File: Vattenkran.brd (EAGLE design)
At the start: 65 x 80 mm, 13 parts, among them Q2 32KHz

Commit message: Replaced crystal
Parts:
- removed Q2: 32KHz, adafruit:TC38H
- added U$2: 32Khz, Semiconductors:SM3
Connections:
- net N$4: now also U$2.P$1; no longer Q2.2
- net N$5: now also U$2.P$2; no longer Q2.1
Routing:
- net N$4: track 6.17 -> 5.39 mm
- net N$5: track 6.08 -> 5.39 mm
- net SUPERCAP: track 5.10 -> 4.45 mm
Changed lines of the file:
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@@
 <element name="C3" library="resistor" library_urn="urn:adsk.eagle:library:348" package="C0805" package3d_urn="urn:adsk.eagle:package:26137/1" value="100nF" x="16.5" y="57.5" rot="MR90"/>
 <element name="LED2" library="led" library_urn="urn:adsk.eagle:library:259" package="LED3MM" package3d_urn="urn:adsk.eagle:package:15797/1" value="GREEN" x="15.63" y="16.18" rot="R90"/>
-<element name="Q2" library="adafruit" package="TC38H" value="32KHz" x="39.23" y="72.42" rot="R180">
-<attribute name="MF" value="" x="39.23" y="72.42" size="1.778" layer="27" rot="R180" display="off"/>
-<attribute name="MPN" value="" x="39.23" y="72.42" size="1.778" layer="27" rot="R180" display="off"/>
-<attribute name="OC_FARNELL" value="unknown" x="39.23" y="72.42" size="1.778" layer="27" rot="R180" display="off"/>
-<attribute name="OC_NEWARK" value="unknown" x="39.23" y="72.42" size="1.778" layer="27" rot="R180" display="off"/>
-</element>
 <element name="R2" library="resistor" library_urn="urn:adsk.eagle:library:348" package="R0805" package3d_urn="urn:adsk.eagle:package:26059/1" value="3K3" x="15.63" y="22.2" rot="MR90"/>
 <element name="SUPERCAP" library="rcl" library_urn="urn:adsk.eagle:library:334" package="ETR2" package3d_urn="urn:adsk.eagle:package:23315/1" value="1F" x="31.8" y="64.02" rot="R180">
@@
 <attribute name="TP_SIGNAL_NAME" value="" x="0" y="60" size="1.778" layer="28" rot="MR0" display="off"/>
 </element>
+<element name="U$2" library="Semiconductors" package="SM3" value="32Khz" x="39.5" y="72" rot="MR270"/>
 </elements>
 <signals>
@@
 <contactref element="U$1" pad="8"/>
 <contactref element="SUPERCAP" pad="+"/>
-<wire x1="37.595" y1="61.14" x2="36.36" y2="61.14" width="0.6096" layer="16"/>
-<wire x1="36.36" y1="61.14" x2="35.34" y2="63.66" width="0.6096" layer="16"/>
-<wire x1="35.34" y1="63.66" x2="34.7" y2="63.66" width="0.6096" layer="16"/>
-<wire x1="34.7" y1="63.66" x2="34.34" y2="64.02" width="0.6096" layer="16"/>
+<wire x1="34.34" y1="64.02" x2="37.22" y2="61.14" width="0.4064" layer="16"/>
+<wire x1="37.22" y1="61.14" x2="37.595" y2="61.14" width="0.4064" layer="16"/>
 </signal>
 <signal name="BT_STATE">
@@
 </signal>
 <signal name="N$4">
-<contactref element="Q2" pad="2"/>
 <contactref element="U$1" pad="2"/>
-<wire x1="38.865" y1="66.86" x2="38.865" y2="71.635" width="0.4064" layer="16"/>
-<wire x1="37.96" y1="72.54" x2="37.96" y2="72.42" width="0.4064" layer="16"/>
-<wire x1="38.865" y1="71.635" x2="37.96" y2="72.54" width="0.4064" layer="16"/>
+<contactref element="U$2" pad="P$1"/>
+<wire x1="38.865" y1="66.86" x2="38.865" y2="69.635" width="0.4064" layer="16"/>
+<wire x1="38.25" y1="70.25" x2="38.25" y2="72" width="0.4064" layer="16"/>
+<wire x1="38.865" y1="69.635" x2="38.25" y2="70.25" width="0.4064" layer="16"/>
 </signal>
 <signal name="N$5">
 <contactref element="U$1" pad="3"/>
-<contactref element="Q2" pad="1"/>
-<wire x1="40.135" y1="66.86" x2="40.135" y2="72.555" width="0.4064" layer="16"/>
-<wire x1="40.135" y1="72.555" x2="40.5" y2="72.42" width="0.4064" layer="16"/>
+<contactref element="U$2" pad="P$2"/>
+<wire x1="40.135" y1="66.86" x2="40.135" y2="69.635" width="0.4064" layer="16"/>
+<wire x1="40.75" y1="70.25" x2="40.75" y2="72" width="0.4064" layer="16"/>
+<wire x1="40.135" y1="69.635" x2="40.75" y2="70.25" width="0.4064" layer="16"/>
 </signal>
 <signal name="VALVE_ENABLE">

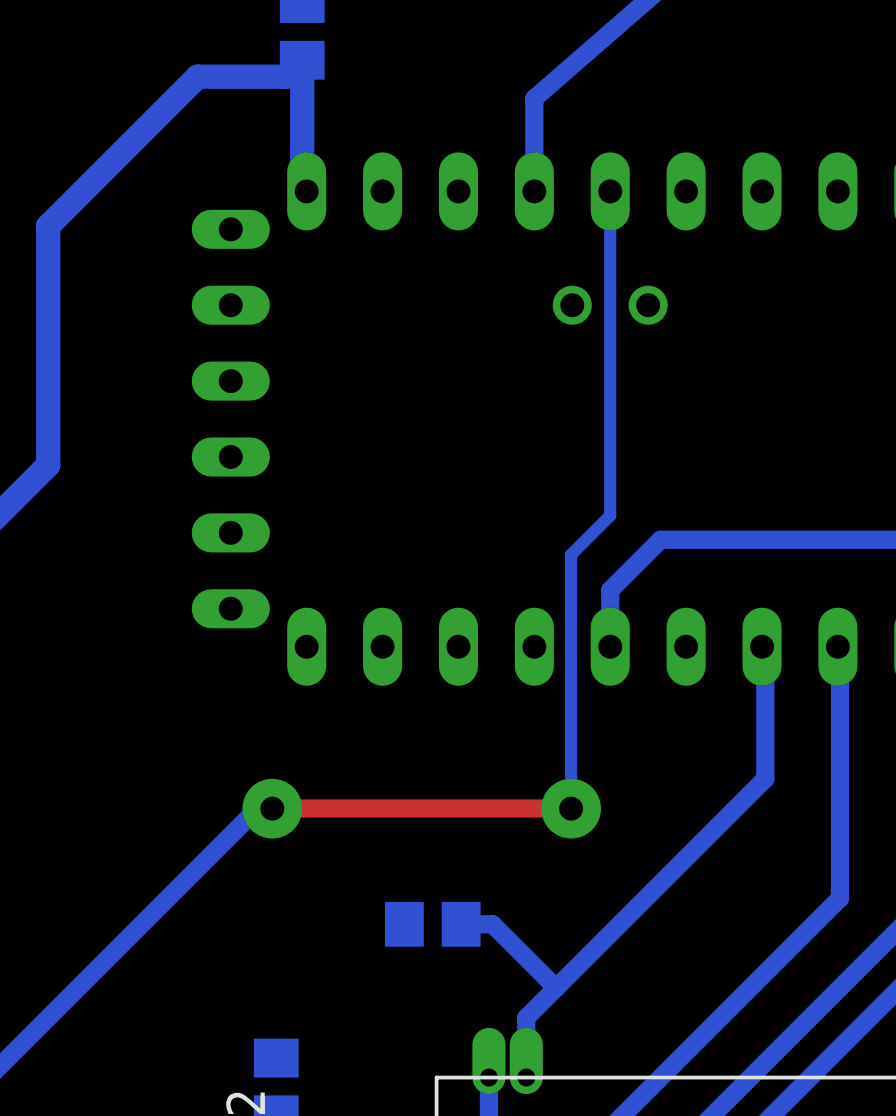
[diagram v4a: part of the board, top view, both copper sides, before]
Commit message: Fixed thermals size
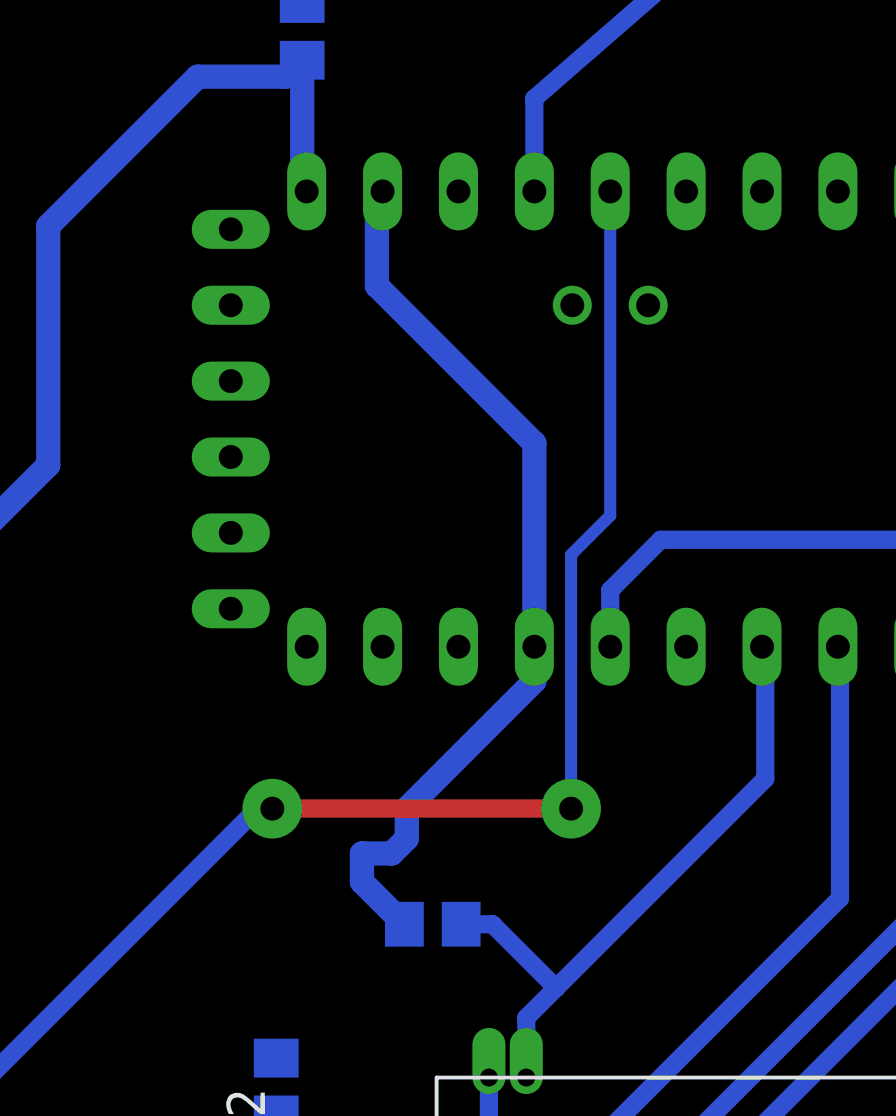
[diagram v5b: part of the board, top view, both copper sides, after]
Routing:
- net GND: track 0.00 -> 30.4 mm
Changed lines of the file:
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@@
 <contactref element="C3" pad="2"/>
 <contactref element="C2" pad="2"/>
-<polygon width="0" layer="16" isolate="1.016">
+<polygon width="0.5" layer="16" isolate="1.016">
 <vertex x="0" y="80"/>
 <vertex x="65" y="80"/>
@@
 <vertex x="0" y="0"/>
 </polygon>
+<wire x1="24.27" y1="36.92" x2="24.27" y2="43.73" width="0.8128" layer="16"/>
+<wire x1="24.27" y1="43.73" x2="19" y2="49" width="0.8128" layer="16"/>
+<wire x1="19" y1="49" x2="19" y2="51.97" width="0.8128" layer="16"/>
+<wire x1="19" y1="51.97" x2="19.19" y2="52.16" width="0.8128" layer="16"/>
+<wire x1="24.27" y1="36.92" x2="24.27" y2="35.77" width="0.8128" layer="16"/>
+<wire x1="20" y1="31.5" x2="20" y2="30.5" width="0.8128" layer="16"/>
+<wire x1="20" y1="30.5" x2="19.5" y2="30" width="0.8128" layer="16"/>
+<wire x1="19.5" y1="30" x2="18.5" y2="30" width="0.8128" layer="16"/>
+<wire x1="18.5" y1="30" x2="18.5" y2="29.05" width="0.8128" layer="16"/>
+<wire x1="18.5" y1="29.05" x2="19.92" y2="27.63" width="0.8128" layer="16"/>
+<wire x1="24.27" y1="35.77" x2="20" y2="31.5" width="0.8128" layer="16"/>
 </signal>
 <signal name="BT_RX">

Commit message: Added cap
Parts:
- added C4: 100µF, resistor:PANASONIC_D
- moved C3 1.58 mm to (16.0, 59.0), turned to 180 degrees
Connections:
- net GND: now also C4.-
- net VCC5: now also C4.+
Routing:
- net VCC5: track 32.5 -> 40.8 mm
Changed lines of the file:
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@@
 <element name="C1" library="resistor" library_urn="urn:adsk.eagle:library:348" package="C0805" package3d_urn="urn:adsk.eagle:package:26137/1" value="100nF" x="32" y="71" rot="MR90"/>
 <element name="C2" library="resistor" library_urn="urn:adsk.eagle:library:348" package="C0805" package3d_urn="urn:adsk.eagle:package:26137/1" value="100nF" x="20.87" y="27.63" rot="MR0"/>
-<element name="C3" library="resistor" library_urn="urn:adsk.eagle:library:348" package="C0805" package3d_urn="urn:adsk.eagle:package:26137/1" value="100nF" x="16.5" y="57.5" rot="MR90"/>
+<element name="C3" library="resistor" library_urn="urn:adsk.eagle:library:348" package="C0805" package3d_urn="urn:adsk.eagle:package:26137/1" value="100nF" x="16" y="59" rot="MR180"/>
 <element name="LED2" library="led" library_urn="urn:adsk.eagle:library:259" package="LED3MM" package3d_urn="urn:adsk.eagle:package:15797/1" value="GREEN" x="15.63" y="16.18" rot="R90"/>
 <element name="R2" library="resistor" library_urn="urn:adsk.eagle:library:348" package="R0805" package3d_urn="urn:adsk.eagle:package:26059/1" value="3K3" x="15.63" y="22.2" rot="MR90"/>
@@
 </element>
 <element name="U$2" library="Semiconductors" package="SM3" value="32Khz" x="39.5" y="72" rot="MR270"/>
+<element name="C4" library="resistor" library_urn="urn:adsk.eagle:library:348" package="PANASONIC_D" package3d_urn="urn:adsk.eagle:package:25914/1" value="100µF" x="18" y="65.5" rot="MR0"/>
 </elements>
 <signals>
@@
 <wire x1="18.5" y1="29.05" x2="19.92" y2="27.63" width="0.8128" layer="16"/>
 <wire x1="24.27" y1="35.77" x2="20" y2="31.5" width="0.8128" layer="16"/>
+<contactref element="C4" pad="-"/>
 </signal>
 <signal name="BT_RX">
@@
 <wire x1="47.5" y1="40.5" x2="49.5" y2="42.5" width="0.6096" layer="16"/>
 <wire x1="49.5" y1="70.5" x2="43" y2="77" width="0.6096" layer="16"/>
-<wire x1="24" y1="77" x2="7" y2="60" width="0.6096" layer="16"/>
+<wire x1="19" y1="77" x2="3" y2="60" width="0.6096" layer="16"/>
 <wire x1="26.81" y1="38.81" x2="28.5" y2="40.5" width="0.6096" layer="16"/>
 <wire x1="49.5" y1="42.5" x2="49.5" y2="70.5" width="0.6096" layer="16"/>
-<wire x1="43" y1="77" x2="24" y2="77" width="0.6096" layer="16"/>
-<wire x1="7" y1="60" x2="0" y2="60" width="0.6096" layer="16"/>
+<wire x1="43" y1="77" x2="19" y2="77" width="0.6096" layer="16"/>
+<wire x1="3" y1="60" x2="0" y2="60" width="0.6096" layer="16"/>
 </signal>
 <signal name="RTC_CE">
@@
 <contactref element="C3" pad="1"/>
 <wire x1="16.65" y1="52.16" x2="16.5" y2="52.31" width="0.8128" layer="16"/>
-<wire x1="16.5" y1="52.31" x2="16.5" y2="56.55" width="0.8128" layer="16"/>
-<wire x1="16.5" y1="56.55" x2="15.95" y2="56" width="0.8128" layer="16"/>
-<wire x1="15.95" y1="56" x2="13" y2="56" width="0.8128" layer="16"/>
+<wire x1="14.95" y1="56" x2="13" y2="56" width="0.8128" layer="16"/>
 <wire x1="13" y1="56" x2="8" y2="51" width="0.8128" layer="16"/>
 <wire x1="8" y1="51" x2="8" y2="43" width="0.8128" layer="16"/>
 <wire x1="8" y1="43" x2="5" y2="40" width="0.8128" layer="16"/>
 <wire x1="5" y1="40" x2="0" y2="40" width="0.8128" layer="16"/>
+<contactref element="C4" pad="+"/>
+<wire x1="16.65" y1="52.16" x2="16.65" y2="54.3" width="0.8128" layer="16"/>
+<wire x1="16.65" y1="54.3" x2="14.95" y2="56" width="0.8128" layer="16"/>
+<wire x1="14.95" y1="56" x2="14.95" y2="58.9" width="0.8128" layer="16"/>
+<wire x1="14.95" y1="58.9" x2="15.05" y2="59" width="0.8128" layer="16"/>
+<wire x1="15.05" y1="59" x2="15.05" y2="64.95" width="0.8128" layer="16"/>
+<wire x1="15.05" y1="64.95" x2="15.6" y2="65.5" width="0.8128" layer="16"/>
 </signal>
 <signal name="VCC33">
